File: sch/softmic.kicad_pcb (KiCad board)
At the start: 2 copper layers, 101.6 x 62.2 mm, 86 parts, among them J1 USB-C Connector, J2 XLR-OUT, J3 AudioJack 3.5mm, P1 4V1, P10 VccPad, P2 4V1, P3 4V1, P4 none, P5 none, P6 none, P7 none, P8 4V1, P9 4V1, Q1 MCP1812BT-033, Q10 ESP32-WROOM, Q11 BC847BS-TP, Q2 MMBFJ201, Q3 CH340G, Q4 BSS64AT116, Q5 OPA1671, Q6 OPA1671, Q7 BQ21040, Q8 MAX11613, Q9 Oled_128_32, SW1 RST, Y1 12MHz

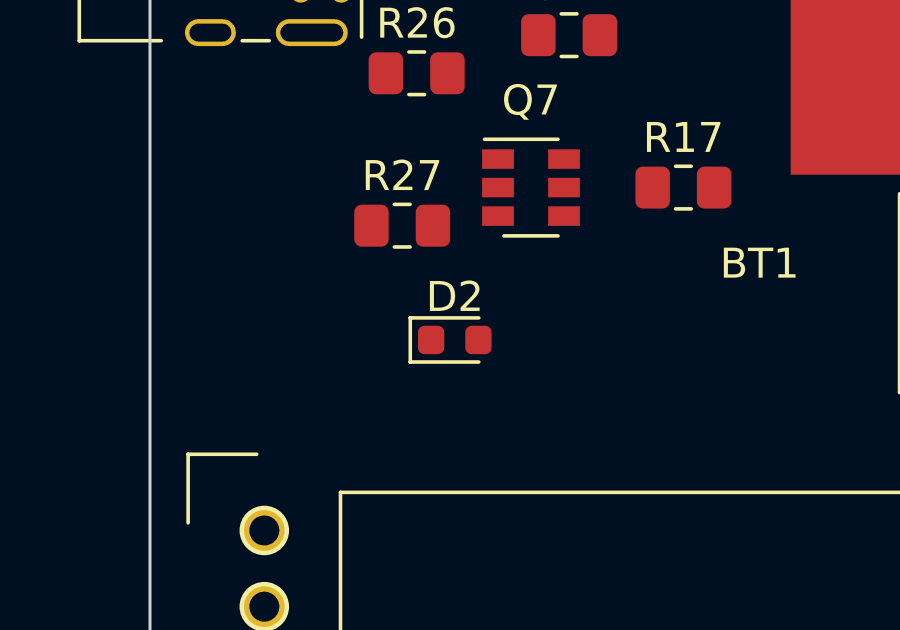
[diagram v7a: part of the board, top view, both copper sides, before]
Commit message: changed LED to red 0805 led
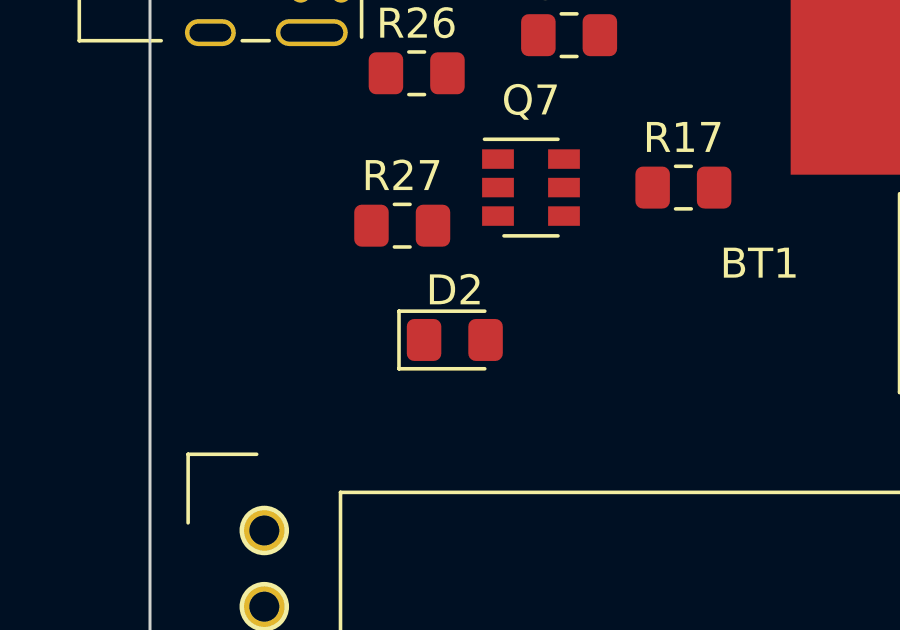
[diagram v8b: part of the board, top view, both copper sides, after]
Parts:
- D2: footprint LED_SMD:LED_0603_1608Metric -> LED_SMD:LED_0805_2012Metric_Pad1.15x1.40mm_HandSolder
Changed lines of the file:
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@@
     (47 F.CrtYd user)
     (48 B.Fab user)
-    (49 F.Fab user)
+    (49 F.Fab user hide)
   )
   (setup
@@
     (add_net "Net-(Q8-Pad4)")
   )
+  (module LED_SMD:LED_0805_2012Metric_Pad1.15x1.40mm_HandSolder (layer F.Cu)
+    (at 99.06 78.74)
+    (descr "LED SMD 0805 (2012 Metric), square (rectangular) end terminal, IPC_7351 nominal, (Body size source: https://docs.google.com/spreadsheets/d/1BsfQQcO9C6DZCsRaXUlFlo91Tg2WpOkGARC1WS5S8t0/edit?usp=sharing), generated with kicad-footprint-generator")
+    (tags "LED handsolder")
+    (attr smd)
+    (fp_text reference D2 (at 0 -1.65) (layer F.SilkS)
+      (effects (font (size 1 1) (thickness 0.15)))
+    )
+    (fp_text value LED (at 0 1.65) (layer F.Fab)
+      (effects (font (size 1 1) (thickness 0.15)))
+    )
+    (fp_text user %R (at 0 0) (layer F.Fab)
+      (effects (font (size 0.5 0.5) (thickness 0.08)))
+    )
+    (fp_line (start 1.85 0.95) (end -1.85 0.95) (layer F.CrtYd) (width 0.05))
+    (fp_line (start 1.85 -0.95) (end 1.85 0.95) (layer F.CrtYd) (width 0.05))
+    (fp_line (start -1.85 -0.95) (end 1.85 -0.95) (layer F.CrtYd) (width 0.05))
+    (fp_line (start -1.85 0.95) (end -1.85 -0.95) (layer F.CrtYd) (width 0.05))
+    (fp_line (start -1.86 0.96) (end 1 0.96) (layer F.SilkS) (width 0.12))
+    (fp_line (start -1.86 -0.96) (end -1.86 0.96) (layer F.SilkS) (width 0.12))
+    (fp_line (start 1 -0.96) (end -1.86 -0.96) (layer F.SilkS) (width 0.12))
+    (fp_line (start 1 0.6) (end 1 -0.6) (layer F.Fab) (width 0.1))
+    (fp_line (start -1 0.6) (end 1 0.6) (layer F.Fab) (width 0.1))
+    (fp_line (start -1 -0.3) (end -1 0.6) (layer F.Fab) (width 0.1))
+    (fp_line (start -0.7 -0.6) (end -1 -0.3) (layer F.Fab) (width 0.1))
+    (fp_line (start 1 -0.6) (end -0.7 -0.6) (layer F.Fab) (width 0.1))
+    (pad 2 smd roundrect (at 1.025 0) (size 1.15 1.4) (layers F.Cu F.Paste F.Mask) (roundrect_rratio 0.217391)
+      (net 16 /BATT))
+    (pad 1 smd roundrect (at -1.025 0) (size 1.15 1.4) (layers F.Cu F.Paste F.Mask) (roundrect_rratio 0.217391)
+      (net 7 "Net-(D2-Pad1)"))
+    (model ${KISYS3DMOD}/LED_SMD.3dshapes/LED_0805_2012Metric.wrl
+      (at (xyz 0 0 0))
+      (scale (xyz 1 1 1))
+      (rotate (xyz 0 0 0))
+    )
+  )
   (module Capacitor_SMD:C_0805_2012Metric_Pad1.15x1.40mm_HandSolder (layer F.Cu)
     (at 123.19 121.92)
@@
       (at (xyz 0 0 0))
       (scale (xyz 1 1 1))
-      (rotate (xyz 0 0 0))
-    )
-  )
-  (module LED_SMD:LED_0603_1608Metric (layer F.Cu)
-    (at 99.06 78.74)
-    (descr "LED SMD 0603 (1608 Metric), square (rectangular) end terminal, IPC_7351 nominal, (Body size source: http://www.tortai-tech.com/upload/download/2011102023233369053.pdf), generated with kicad-footprint-generator")
-    (tags diode)
-    (attr smd)
-    (fp_text reference D2 (at 0 -1.43) (layer F.SilkS)
-      (effects (font (size 1 1) (thickness 0.15)))
-    )
-    (fp_text value LED (at 0 1.43) (layer F.Fab)
-      (effects (font (size 1 1) (thickness 0.15)))
-    )
-    (fp_text user %R (at 0 0) (layer F.Fab)
-      (effects (font (size 0.4 0.4) (thickness 0.06)))
-    )
-    (fp_line (start 1.48 0.73) (end -1.48 0.73) (layer F.CrtYd) (width 0.05))
-    (fp_line (start 1.48 -0.73) (end 1.48 0.73) (layer F.CrtYd) (width 0.05))
-    (fp_line (start -1.48 -0.73) (end 1.48 -0.73) (layer F.CrtYd) (width 0.05))
-    (fp_line (start -1.48 0.73) (end -1.48 -0.73) (layer F.CrtYd) (width 0.05))
-    (fp_line (start -1.485 0.735) (end 0.8 0.735) (layer F.SilkS) (width 0.12))
-    (fp_line (start -1.485 -0.735) (end -1.485 0.735) (layer F.SilkS) (width 0.12))
-    (fp_line (start 0.8 -0.735) (end -1.485 -0.735) (layer F.SilkS) (width 0.12))
-    (fp_line (start 0.8 0.4) (end 0.8 -0.4) (layer F.Fab) (width 0.1))
-    (fp_line (start -0.8 0.4) (end 0.8 0.4) (layer F.Fab) (width 0.1))
-    (fp_line (start -0.8 -0.1) (end -0.8 0.4) (layer F.Fab) (width 0.1))
-    (fp_line (start -0.5 -0.4) (end -0.8 -0.1) (layer F.Fab) (width 0.1))
-    (fp_line (start 0.8 -0.4) (end -0.5 -0.4) (layer F.Fab) (width 0.1))
-    (pad 2 smd roundrect (at 0.7875 0) (size 0.875 0.95) (layers F.Cu F.Paste F.Mask) (roundrect_rratio 0.25)
-      (net 16 /BATT))
-    (pad 1 smd roundrect (at -0.7875 0) (size 0.875 0.95) (layers F.Cu F.Paste F.Mask) (roundrect_rratio 0.25)
-      (net 7 "Net-(D2-Pad1)"))
-    (model ${KISYS3DMOD}/LED_SMD.3dshapes/LED_0603_1608Metric.wrl
-      (at (xyz 0 0 0))
-      (scale (xyz 1 1 1))
